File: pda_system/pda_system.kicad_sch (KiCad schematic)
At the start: 0 parts

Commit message: added the symbol for the microcontroller to the schematic
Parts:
- added U1: STM32F103C8Tx, Package_QFP:LQFP-48_7x7mm_P0.5mm, symbol MCU_ST_STM32F1:STM32F103C8Tx
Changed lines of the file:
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@@
 (kicad_sch (version 20211123) (generator eeschema)
   (paper "A4")
+  (symbol (lib_id "MCU_ST_STM32F1:STM32F103C8Tx") (at 52.07 73.66 0) (unit 1)
+    (in_bom yes) (on_board yes) (fields_autoplaced)
+    (property "Reference" "U1" (id 0) (at 56.6294 111.76 0)
+      (effects (font (size 1.27 1.27)) (justify left))
+    )
+    (property "Value" "STM32F103C8Tx" (id 1) (at 56.6294 114.3 0)
+      (effects (font (size 1.27 1.27)) (justify left))
+    )
+    (property "Footprint" "Package_QFP:LQFP-48_7x7mm_P0.5mm" (id 2) (at 36.83 109.22 0)
+      (effects (font (size 1.27 1.27)) (justify right) hide)
+    )
+    (property "Datasheet" "http://www.st.com/st-web-ui/static/active/en/resource/technical/document/datasheet/CD00161566.pdf" (id 3) (at 52.07 73.66 0)
+      (effects (font (size 1.27 1.27)) hide)
+    )
+    (pin "1")
+    (pin "10")
+    (pin "11")
+    (pin "12")
+    (pin "13")
+    (pin "14")
+    (pin "15")
+    (pin "16")
+    (pin "17")
+    (pin "18")
+    (pin "19")
+    (pin "2")
+    (pin "20")
+    (pin "21")
+    (pin "22")
+    (pin "23")
+    (pin "24")
+    (pin "25")
+    (pin "26")
+    (pin "27")
+    (pin "28")
+    (pin "29")
+    (pin "3")
+    (pin "30")
+    (pin "31")
+    (pin "32")
+    (pin "33")
+    (pin "34")
+    (pin "35")
+    (pin "36")
+    (pin "37")
+    (pin "38")
+    (pin "39")
+    (pin "4")
+    (pin "40")
+    (pin "41")
+    (pin "42")
+    (pin "43")
+    (pin "44")
+    (pin "45")
+    (pin "46")
+    (pin "47")
+    (pin "48")
+    (pin "5")
+    (pin "6")
+    (pin "7")
+    (pin "8")
+    (pin "9")
+  )
   (sheet_instances
     (path "/" (page "1"))
   )
+  (symbol_instances
+    (path "/240c10af-51b5-420e-a6f4-a2c8f5db1db5"
+      (reference "U1") (unit 1) (value "STM32F103C8Tx") (footprint "Package_QFP:LQFP-48_7x7mm_P0.5mm")
+    )
+  )
 )

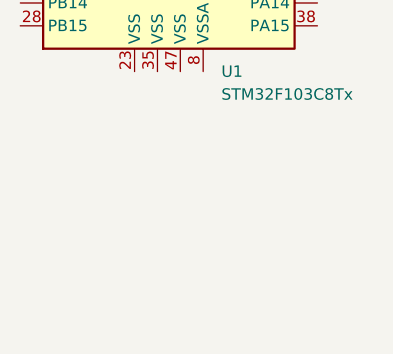
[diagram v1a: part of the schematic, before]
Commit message: updated with crystal oscilator and the HC-49 footprint
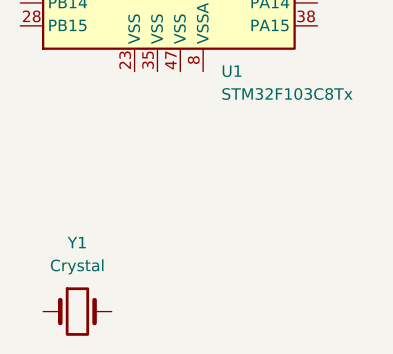
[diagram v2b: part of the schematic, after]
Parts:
- added Y1: Crystal, Crystal:Crystal_HC49-4H_Vertical, symbol Device:Crystal
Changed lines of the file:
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@@
     (pin "9")
+  )
+  (symbol (lib_id "Device:Crystal") (at 40.64 138.43 0) (unit 1)
+    (in_bom yes) (on_board yes) (fields_autoplaced)
+    (property "Reference" "Y1" (id 0) (at 40.64 130.81 0))
+    (property "Value" "Crystal" (id 1) (at 40.64 133.35 0))
+    (property "Footprint" "Crystal:Crystal_HC49-4H_Vertical" (id 2) (at 40.64 138.43 0)
+      (effects (font (size 1.27 1.27)) hide)
+    )
+    (property "Datasheet" "~" (id 3) (at 40.64 138.43 0)
+      (effects (font (size 1.27 1.27)) hide)
+    )
+    (pin "1")
+    (pin "2")
   )
   (sheet_instances
@@
       (reference "U1") (unit 1) (value "STM32F103C8Tx") (footprint "Package_QFP:LQFP-48_7x7mm_P0.5mm")
     )
+    (path "/7550a2ff-4cfd-4300-8cc1-1407b01c45e0"
+      (reference "Y1") (unit 1) (value "Crystal") (footprint "Crystal:Crystal_HC49-4H_Vertical")
+    )
   )

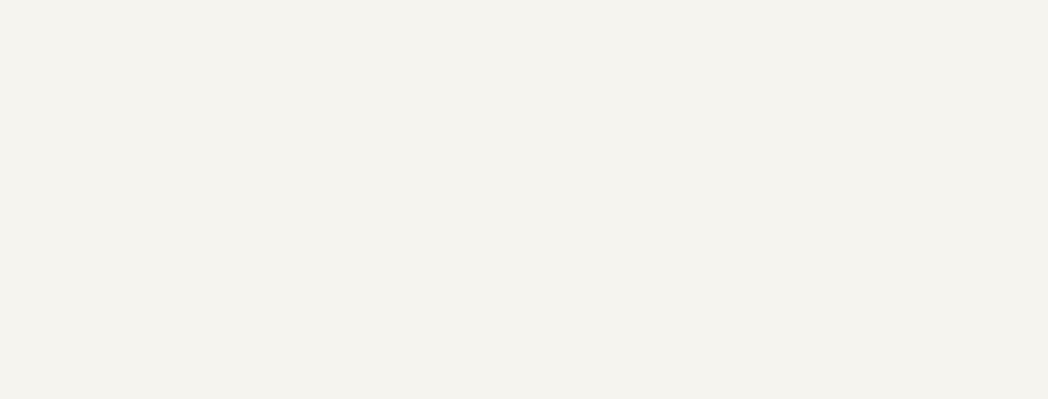
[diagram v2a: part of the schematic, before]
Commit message: Added the CAN tranceiver along with a screw terminal connector to the schematic parts
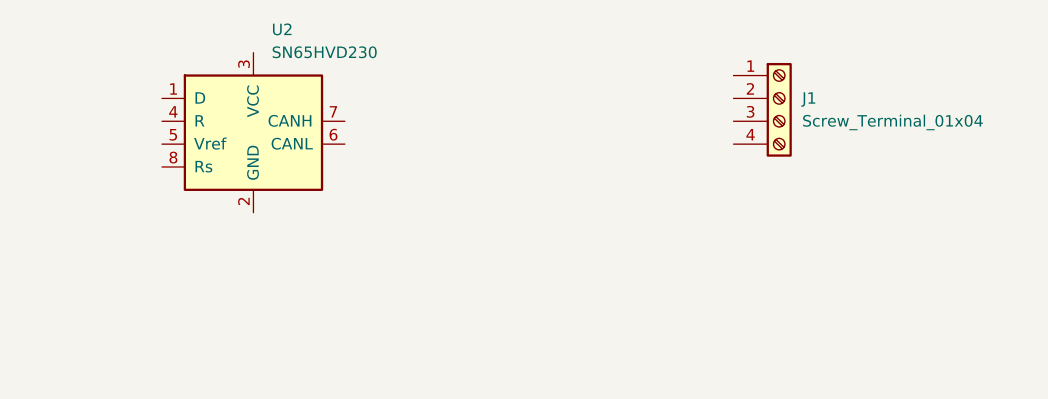
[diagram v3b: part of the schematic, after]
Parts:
- added J1: Screw_Terminal_01x04, symbol Connector:Screw_Terminal_01x04
- added U2: SN65HVD230, Package_SO:SOIC-8_3.9x4.9mm_P1.27mm, symbol Interface_CAN_LIN:SN65HVD230
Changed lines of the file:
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@@
     (pin "2")
+  )
+  (symbol (lib_id "Interface_CAN_LIN:SN65HVD230") (at 120.65 38.1 0) (unit 1)
+    (in_bom yes) (on_board yes) (fields_autoplaced)
+    (property "Reference" "U2" (id 0) (at 122.6694 27.94 0)
+      (effects (font (size 1.27 1.27)) (justify left))
+    )
+    (property "Value" "SN65HVD230" (id 1) (at 122.6694 30.48 0)
+      (effects (font (size 1.27 1.27)) (justify left))
+    )
+    (property "Footprint" "Package_SO:SOIC-8_3.9x4.9mm_P1.27mm" (id 2) (at 120.65 50.8 0)
+      (effects (font (size 1.27 1.27)) hide)
+    )
+    (property "Datasheet" "http://www.ti.com/lit/ds/symlink/sn65hvd230.pdf" (id 3) (at 118.11 27.94 0)
+      (effects (font (size 1.27 1.27)) hide)
+    )
+    (pin "1")
+    (pin "2")
+    (pin "3")
+    (pin "4")
+    (pin "5")
+    (pin "6")
+    (pin "7")
+    (pin "8")
+  )
+  (symbol (lib_id "Connector:Screw_Terminal_01x04") (at 179.07 35.56 0) (unit 1)
+    (in_bom yes) (on_board yes) (fields_autoplaced)
+    (property "Reference" "J1" (id 0) (at 181.61 35.5599 0)
+      (effects (font (size 1.27 1.27)) (justify left))
+    )
+    (property "Value" "Screw_Terminal_01x04" (id 1) (at 181.61 38.0999 0)
+      (effects (font (size 1.27 1.27)) (justify left))
+    )
+    (property "Footprint" "" (id 2) (at 179.07 35.56 0)
+      (effects (font (size 1.27 1.27)) hide)
+    )
+    (property "Datasheet" "~" (id 3) (at 179.07 35.56 0)
+      (effects (font (size 1.27 1.27)) hide)
+    )
+    (pin "1")
+    (pin "2")
+    (pin "3")
+    (pin "4")
   )
   (sheet_instances
@@
   )
   (symbol_instances
+    (path "/eb9b5d48-4ac2-4e9d-9da1-616f34dc2419"
+      (reference "J1") (unit 1) (value "Screw_Terminal_01x04") (footprint "")
+    )
     (path "/240c10af-51b5-420e-a6f4-a2c8f5db1db5"
       (reference "U1") (unit 1) (value "STM32F103C8Tx") (footprint "Package_QFP:LQFP-48_7x7mm_P0.5mm")
     )
+    (path "/88610282-a92d-4c3d-917a-ea95d59e0759"
+      (reference "U2") (unit 1) (value "SN65HVD230") (footprint "Package_SO:SOIC-8_3.9x4.9mm_P1.27mm")
+    )
     (path "/7550a2ff-4cfd-4300-8cc1-1407b01c45e0"

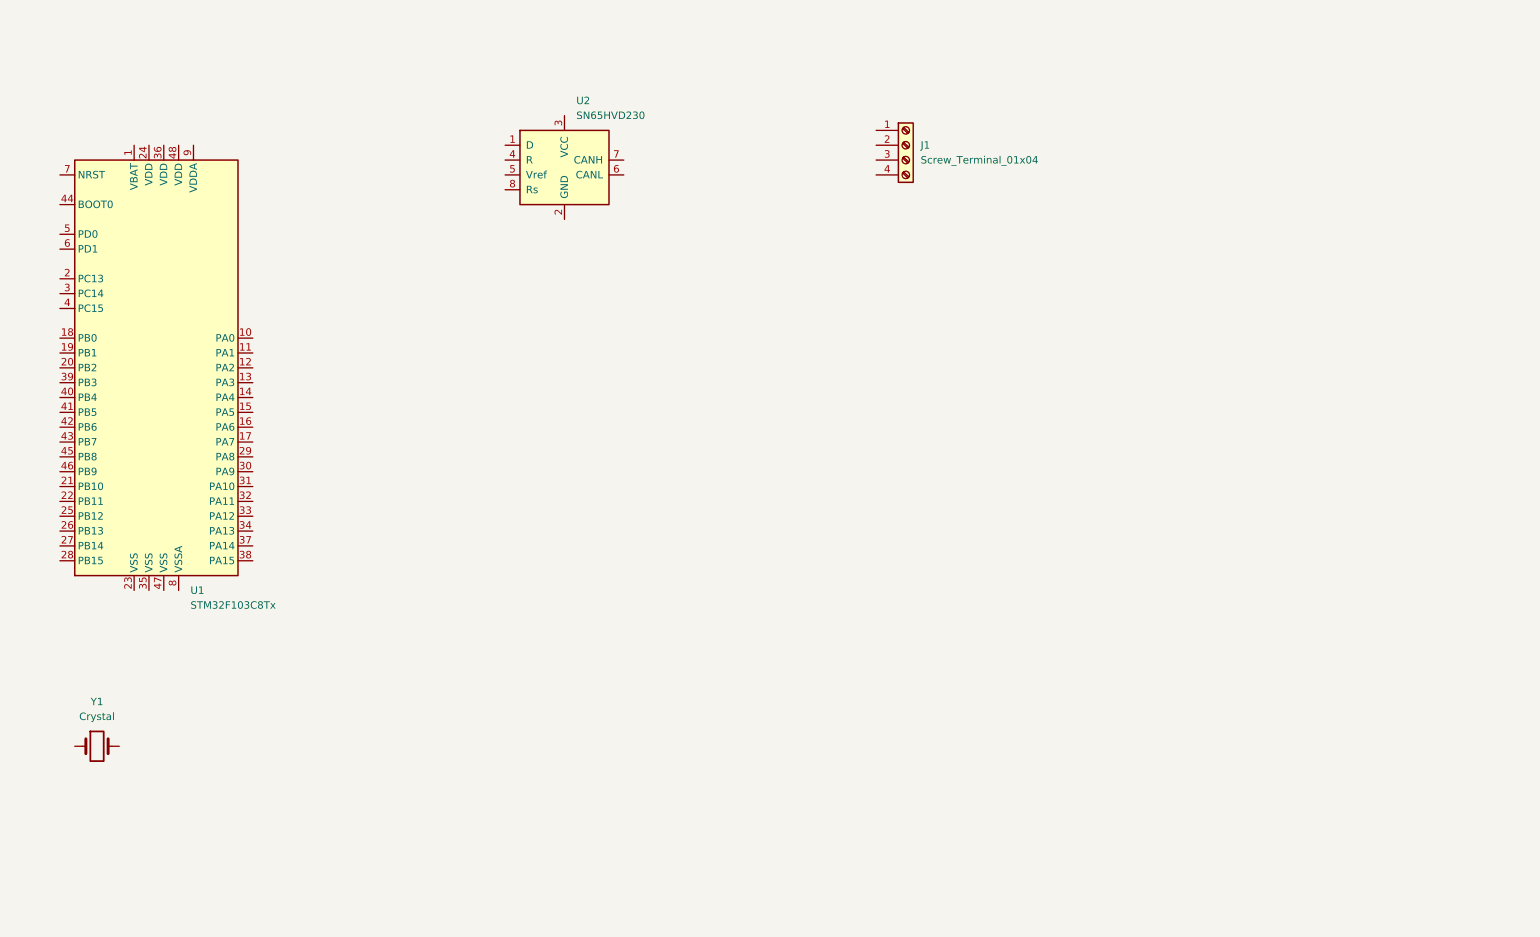
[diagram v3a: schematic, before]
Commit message: updated with external crystal oscilator
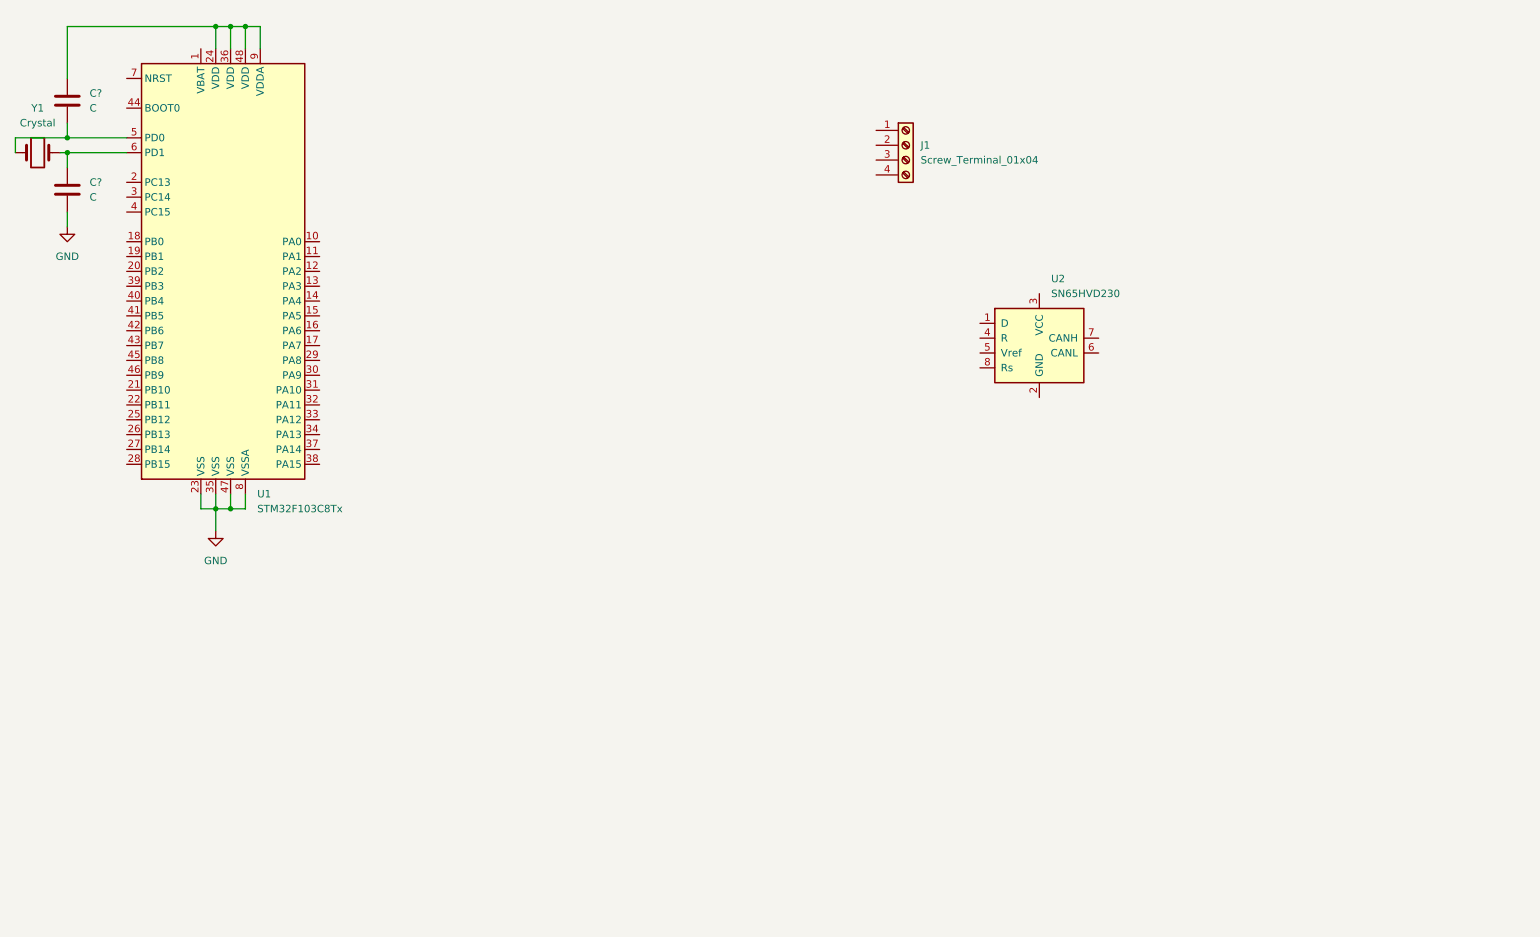
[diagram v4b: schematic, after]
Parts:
- added C? (x2): C, symbol Device:C
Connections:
- net GND: now reaches U1.23 (VSS)
- net GND: now also U1.35 (VSS), U1.47 (VSS), U1.8 (VSSA), C?.2
- net at U1.24 (VDD): now also U1.36 (VDD), U1.48 (VDD), U1.9 (VDDA), C?.1
- net at U1.5 (PD0): now also Y1.1, C?.2
- net at U1.6 (PD1): now also Y1.2, C?.1
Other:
- moved on the sheet: U1, U2, Y1

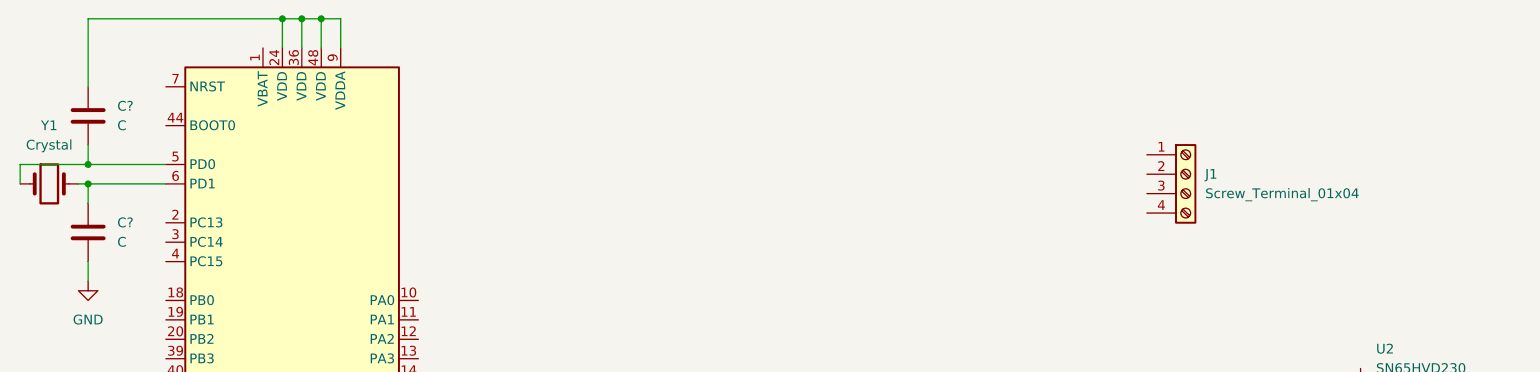
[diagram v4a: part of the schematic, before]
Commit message: Added a buck converter IC to BOM/parts list
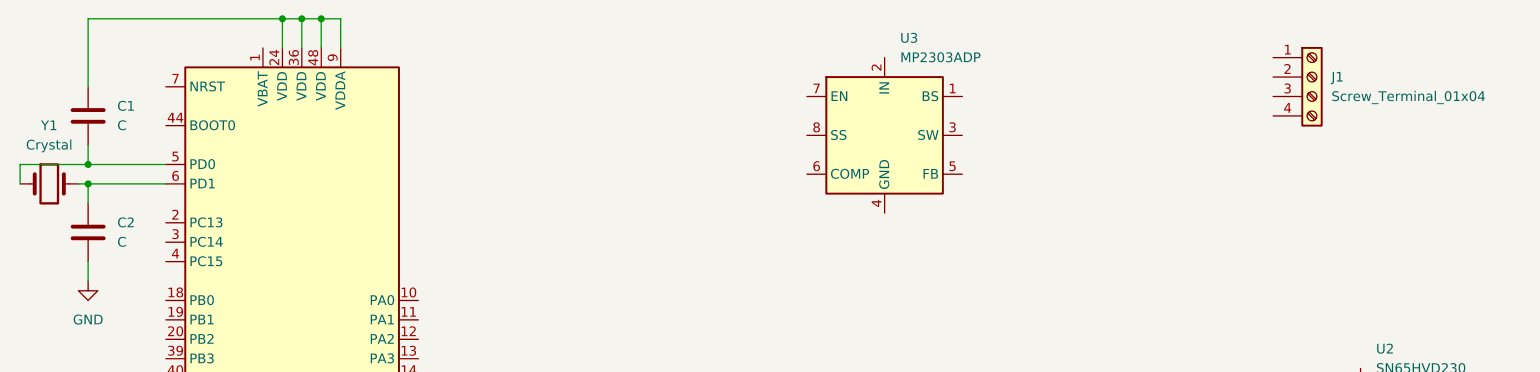
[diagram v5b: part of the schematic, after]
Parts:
- added U3: MP2303ADP, Package_DIP:DIP-8_W7.62mm, symbol Regulator_Switching:MP2303ADP
- gave numbers to parts that had none: 2
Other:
- moved on the sheet: J1
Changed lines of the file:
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@@
   (symbol (lib_id "Device:C") (at 35.56 43.18 0) (unit 1)
     (in_bom yes) (on_board yes) (fields_autoplaced)
-    (property "Reference" "C?" (id 0) (at 39.37 41.9099 0)
+    (property "Reference" "C2" (id 0) (at 39.37 41.9099 0)
       (effects (font (size 1.27 1.27)) (justify left))
     )
@@
     (pin "1")
     (pin "2")
+  )
+  (symbol (lib_id "Regulator_Switching:MP2303ADP") (at 139.7 30.48 0) (unit 1)
+    (in_bom yes) (on_board yes) (fields_autoplaced)
+    (property "Reference" "U3" (id 0) (at 141.7194 17.78 0)
+      (effects (font (size 1.27 1.27)) (justify left))
+    )
+    (property "Value" "MP2303ADP" (id 1) (at 141.7194 20.32 0)
+      (effects (font (size 1.27 1.27)) (justify left))
+    )
+    (property "Footprint" "Package_DIP:DIP-8_W7.62mm" (id 2) (at 139.7 33.02 0)
+      (effects (font (size 1.27 1.27)) hide)
+    )
+    (property "Datasheet" "https://www.monolithicpower.com/pub/media/document/MP2303A_r1.1.pdf" (id 3) (at 139.7 33.02 0)
+      (effects (font (size 1.27 1.27)) hide)
+    )
+    (pin "1")
+    (pin "2")
+    (pin "3")
+    (pin "4")
+    (pin "5")
+    (pin "6")
+    (pin "7")
+    (pin "8")
   )
   (symbol (lib_id "MCU_ST_STM32F1:STM32F103C8Tx") (at 63.5 57.15 0) (unit 1)
@@
   (symbol (lib_id "Device:C") (at 35.56 27.94 0) (unit 1)
     (in_bom yes) (on_board yes) (fields_autoplaced)
-    (property "Reference" "C?" (id 0) (at 39.37 26.6699 0)
+    (property "Reference" "C1" (id 0) (at 39.37 26.6699 0)
       (effects (font (size 1.27 1.27)) (justify left))
     )
@@
     (pin "2")
   )
-  (symbol (lib_id "Connector:Screw_Terminal_01x04") (at 179.07 35.56 0) (unit 1)
-    (in_bom yes) (on_board yes) (fields_autoplaced)
-    (property "Reference" "J1" (id 0) (at 181.61 35.5599 0)
-      (effects (font (size 1.27 1.27)) (justify left))
-    )
-    (property "Value" "Screw_Terminal_01x04" (id 1) (at 181.61 38.0999 0)
-      (effects (font (size 1.27 1.27)) (justify left))
-    )
-    (property "Footprint" "" (id 2) (at 179.07 35.56 0)
-      (effects (font (size 1.27 1.27)) hide)
-    )
-    (property "Datasheet" "~" (id 3) (at 179.07 35.56 0)
+  (symbol (lib_id "Connector:Screw_Terminal_01x04") (at 195.58 22.86 0) (unit 1)
+    (in_bom yes) (on_board yes) (fields_autoplaced)
+    (property "Reference" "J1" (id 0) (at 198.12 22.8599 0)
+      (effects (font (size 1.27 1.27)) (justify left))
+    )
+    (property "Value" "Screw_Terminal_01x04" (id 1) (at 198.12 25.3999 0)
+      (effects (font (size 1.27 1.27)) (justify left))
+    )
+    (property "Footprint" "" (id 2) (at 195.58 22.86 0)
+      (effects (font (size 1.27 1.27)) hide)
+    )
+    (property "Datasheet" "~" (id 3) (at 195.58 22.86 0)
       (effects (font (size 1.27 1.27)) hide)
     )
@@
       (reference "#PWR?") (unit 1) (value "GND") (footprint "")
     )
+    (path "/e4b930d4-e153-4821-a72c-c924db7df444"
+      (reference "C1") (unit 1) (value "C") (footprint "")
+    )
     (path "/065f4e5e-6a63-4d78-b2c5-cfc02e75af73"
-      (reference "C?") (unit 1) (value "C") (footprint "")
-    )
-    (path "/e4b930d4-e153-4821-a72c-c924db7df444"
-      (reference "C?") (unit 1) (value "C") (footprint "")
+      (reference "C2") (unit 1) (value "C") (footprint "")
     )
     (path "/eb9b5d48-4ac2-4e9d-9da1-616f34dc2419"
@@
       (reference "U2") (unit 1) (value "SN65HVD230") (footprint "Package_SO:SOIC-8_3.9x4.9mm_P1.27mm")
     )
+    (path "/1328d75a-2533-4acd-8563-00b5d0f1dd9b"
+      (reference "U3") (unit 1) (value "MP2303ADP") (footprint "Package_DIP:DIP-8_W7.62mm")
+    )
     (path "/7550a2ff-4cfd-4300-8cc1-1407b01c45e0"
